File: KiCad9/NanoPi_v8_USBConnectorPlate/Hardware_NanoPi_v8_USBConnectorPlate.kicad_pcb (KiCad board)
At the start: 2 copper layers, 16 x 60 mm, 17 parts, among them J10 Conn_01x04, J11 Conn_01x02, J12 Conn_01x02, J2 USB_Host_Data_02x02, J3 USB_Host_Data_02x02, J4 USB_Power_02x02, J5 Conn_01x03, J6 Conn_01x09, J8 Conn_01x09, U1 USBLC6-2P6, U2 USBLC6-2P6, U3 USBLC6-2P6

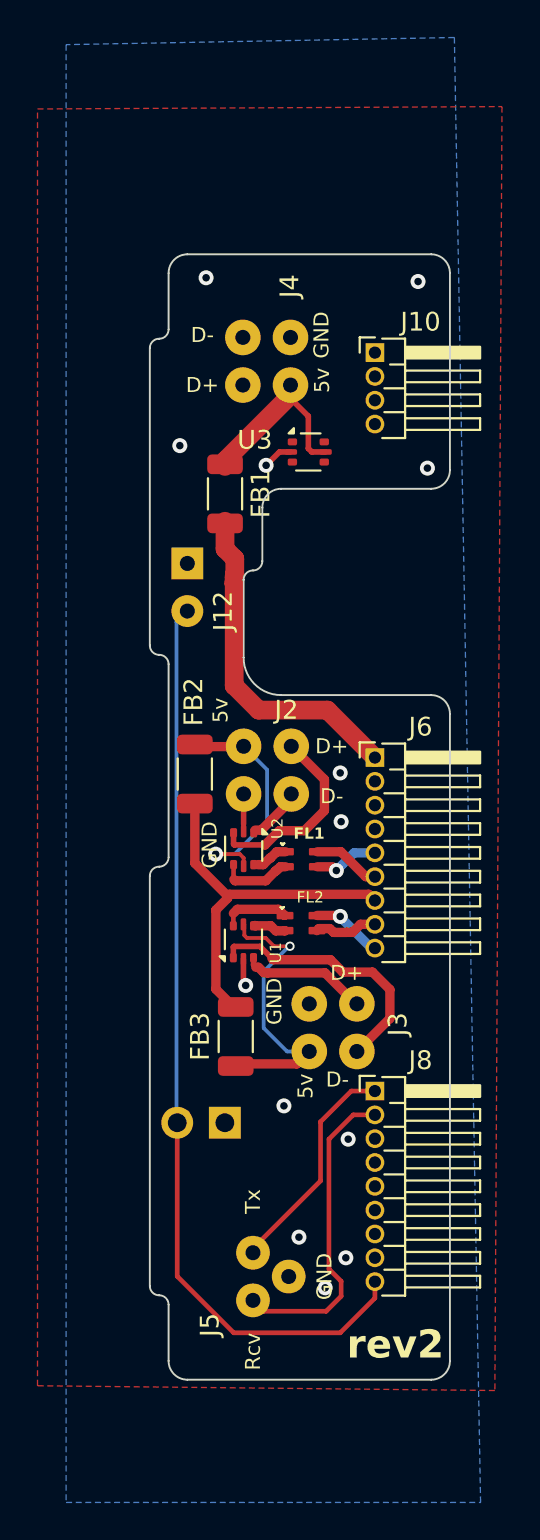
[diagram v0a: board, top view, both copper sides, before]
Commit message: add bom
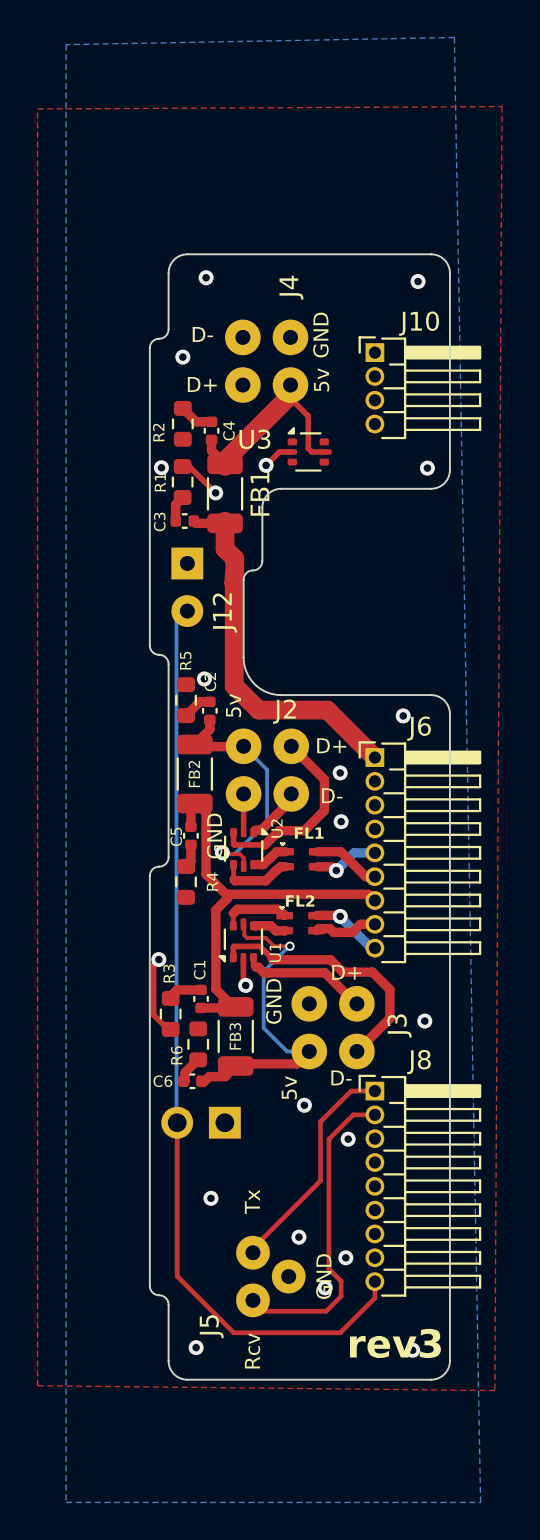
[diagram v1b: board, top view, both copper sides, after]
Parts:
- added C1: 4.7 uF, Capacitor_SMD:C_0402_1005Metric, F.Cu at (104.7, 87.2)
- added C2: 4.7 uF, Capacitor_SMD:C_0402_1005Metric, F.Cu at (105.2, 71.8)
- added C3: 4.7 uF, Capacitor_SMD:C_0402_1005Metric, F.Cu at (103.9, 61.7)
- added C4: 4.7 uF, Capacitor_SMD:C_0402_1005Metric, F.Cu at (105.3, 56.9)
- added C5: 4.7 uF, Capacitor_SMD:C_0402_1005Metric, F.Cu at (104.2, 78.5)
- added C6: 4.7 uF, Capacitor_SMD:C_0402_1005Metric, F.Cu at (104.3, 91.6)
- added R1: 4.7 Ohm, Resistor_SMD:R_0603_1608Metric, F.Cu at (103.8, 59.6)
- added R2: 4.7 Ohm, Resistor_SMD:R_0603_1608Metric, F.Cu at (103.8, 56.5)
- added R3: 4.7 Ohm, Resistor_SMD:R_0603_1608Metric, F.Cu at (103.1, 88.0)
- added R4: 4.7 Ohm, Resistor_SMD:R_0603_1608Metric, F.Cu at (103.9, 81.0)
- added R5: 4.7 Ohm, Resistor_SMD:R_0603_1608Metric, F.Cu at (103.9, 71.3)
- added R6: 4.7 Ohm, Resistor_SMD:R_0603_1608Metric, F.Cu at (104.6, 89.6)
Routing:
- net GND: track 5.07 -> 11.7 mm, vias 13 -> 22
- net VDD_5V: track 20.5 -> 23.7 mm
- net VDD_5V_OUT2: track 15.4 -> 17.6 mm
- net Net-(C1-Pad2): track 0.00 -> 1.91 mm
- net Net-(C4-Pad2): track 0.00 -> 1.83 mm
- net VBUS: track 18.1 -> 19.8 mm
- net VBUS_IN: track 10.6 -> 12.2 mm
- net Net-(C2-Pad2): track 0.00 -> 1.57 mm
- net Net-(C6-Pad2): track 0.00 -> 1.53 mm
- net Net-(C3-Pad1): track 0.00 -> 1.41 mm
- net Net-(C5-Pad2): track 0.00 -> 1.26 mm
- net VDD_5V_OUT1: track 13.7 -> 14.6 mm
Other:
- board text added: "rev3"
- board text removed: "rev2"

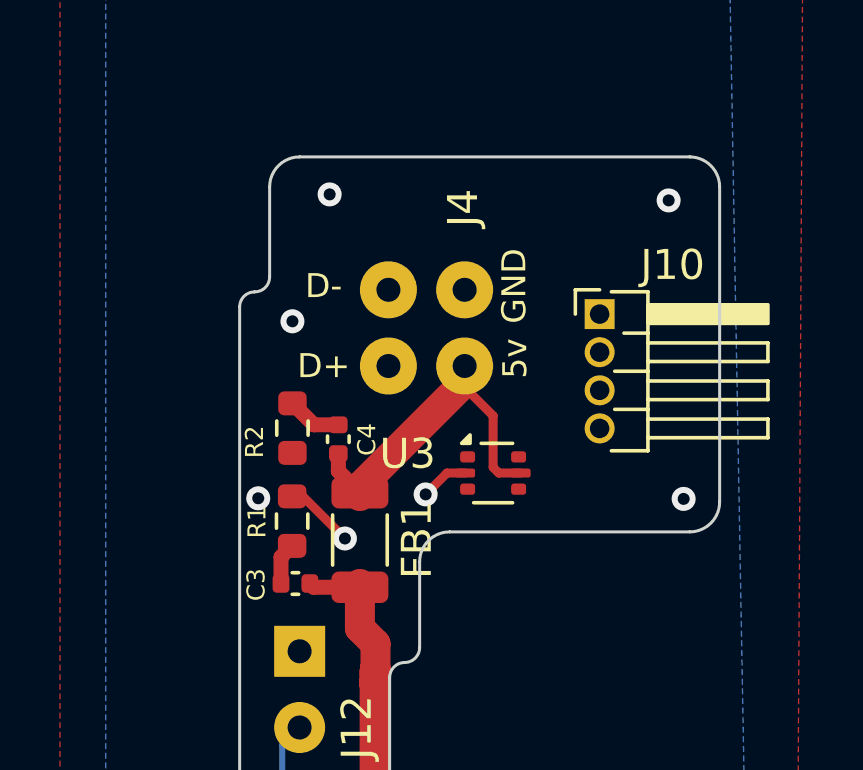
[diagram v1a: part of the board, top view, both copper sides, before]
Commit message: add 3d of wifiboard
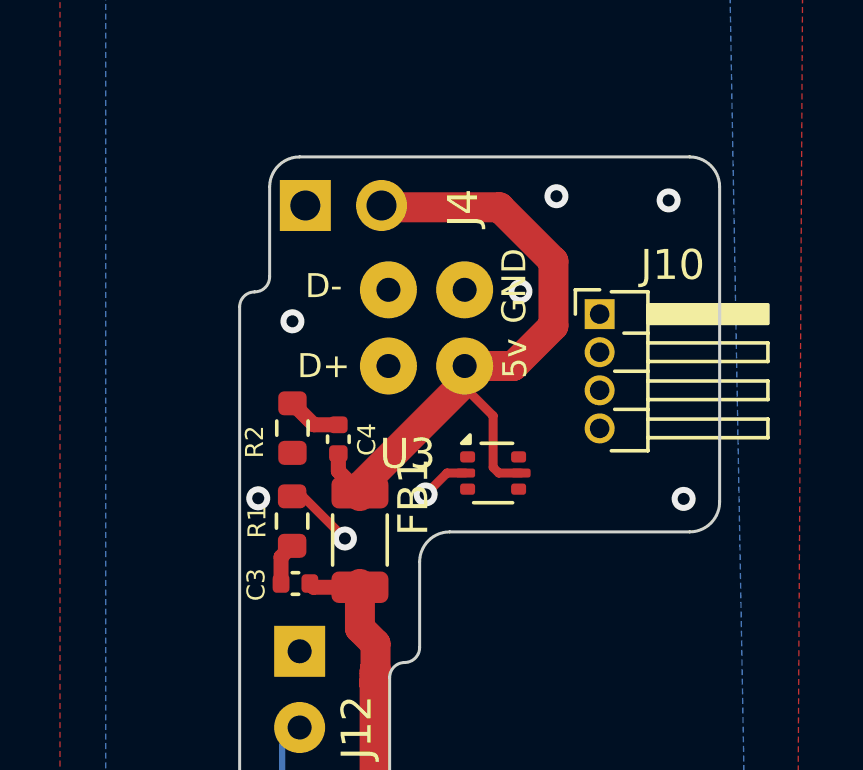
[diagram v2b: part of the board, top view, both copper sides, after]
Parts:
- added J1: Conn_01x02, Connector_PinHeader_2.54mm:PinHeader_1x02_P2.54mm_Horizontal, B.Cu at (104.2, 49.1)
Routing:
- net VBUS_IN: track 12.2 -> 24.5 mm
- net GND: vias 22 -> 23

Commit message: etc
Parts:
- removed FL1, FL2: Choke_CommonMode_FerriteCore_1243, WiRoc:0805_CommonModeChoke
- added FL3: Choke_CommonMode_FerriteCore_1423, WiRoc:0805_CommonModeChoke_1423, F.Cu at (110.0, 79.8)
- added FL4: Choke_CommonMode_FerriteCore_1423, WiRoc:0805_CommonModeChoke_1423, F.Cu at (110.0, 83.0)
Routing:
- net VDD_5V_OUT2: track 17.6 -> 18.9 mm
- net VDD_5V_OUT1: track 14.6 -> 15.5 mm
- net GND: vias 23 -> 24

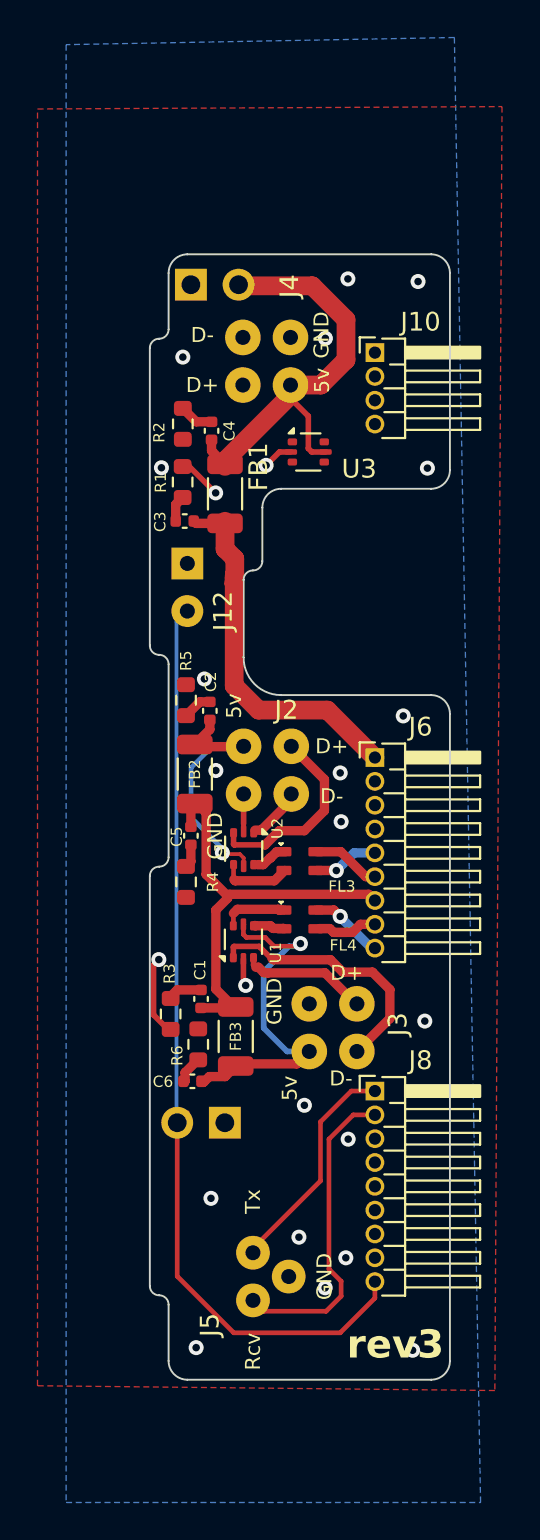
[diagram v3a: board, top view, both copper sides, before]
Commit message: change to use smaller pin holes
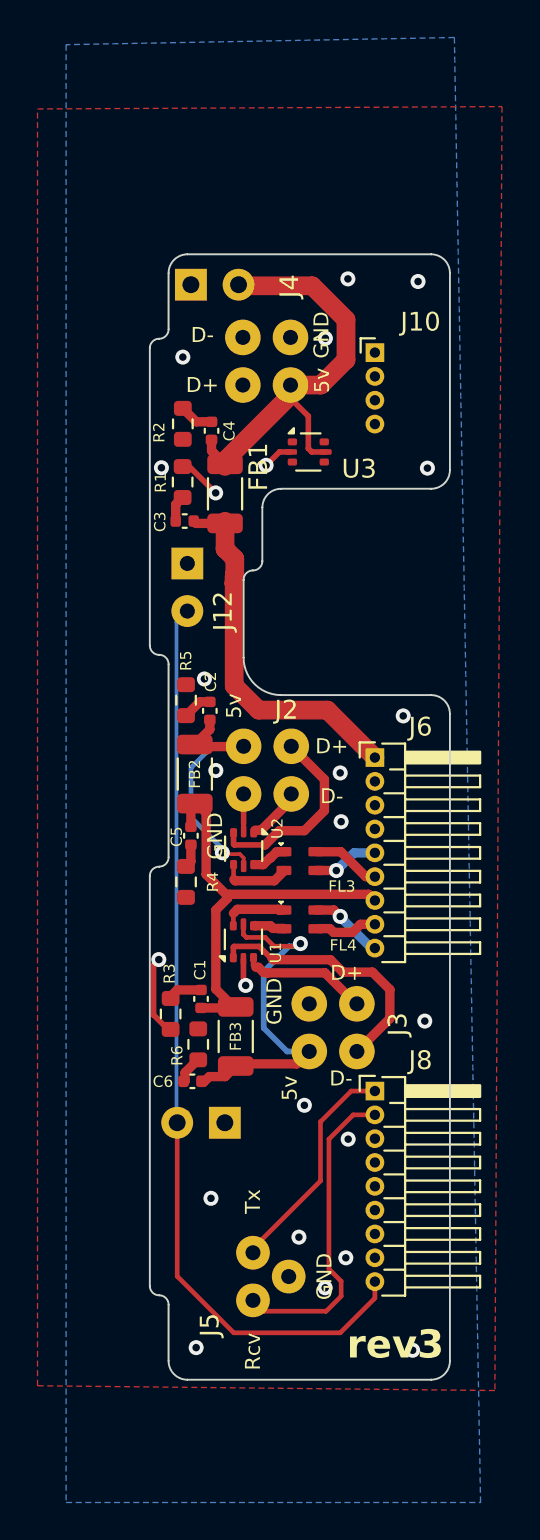
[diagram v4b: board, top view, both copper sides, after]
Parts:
- J1, J11: footprint Connector_PinHeader_2.54mm:PinHeader_1x02_P2.54mm_Horizontal -> WiRoc:PinHeader_1x02_P2.54mm_Horizontal
- J10: footprint Connector_PinHeader_1.27mm:PinHeader_1x04_P1.27mm_Horizontal -> WiRoc:PinHeader_1x04_P1.27mm_Horizontal
- J6, J8: footprint Connector_PinHeader_1.27mm:PinHeader_1x09_P1.27mm_Horizontal -> WiRoc:PinHeader_1x09_P1.27mm_Horizontal

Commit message: add ethernet etc
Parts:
- added C10: 100nF, Capacitor_SMD:C_0402_1005Metric, F.Cu at (104.0, 95.2)
- added C11: 100nF, Capacitor_SMD:C_0402_1005Metric, F.Cu at (104.0, 99.0)
- added C12: 100 nF, Capacitor_SMD:C_0402_1005Metric, B.Cu at (115.8, 102.7)
- added C13: 100 nF, Capacitor_SMD:C_0402_1005Metric, B.Cu at (111.2, 94.3)
- added C14: 1 nF 2kV, Capacitor_SMD:C_1206_3216Metric, B.Cu at (104.3, 105.0)
- added C7: 100nF, Capacitor_SMD:C_0402_1005Metric, F.Cu at (108.3, 93.7)
- added C8: 100nF, Capacitor_SMD:C_0402_1005Metric, F.Cu at (110.7, 93.7)
- added C9: 100nF, Capacitor_SMD:C_0402_1005Metric, F.Cu at (104.0, 97.1)
- added FB4: FerriteBead, Inductor_SMD:L_1206_3216Metric, B.Cu at (103.2, 100.1)
- added FL1: MCZ1210AH900L2TA0G, WiRoc:MCZ1210AH_L2_TDK, B.Cu at (110.2, 105.3)
- added FL2: MCZ1210AH900L2TA0G, WiRoc:MCZ1210AH_L2_TDK, B.Cu at (105.3, 97.7)
- added NT1: NetTie_2, WiRoc:NetTie-2_SMD_Pad0.3mm, B.Cu at (108.4, 103.8)
- added NT2: NetTie_2, WiRoc:NetTie-2_SMD_Pad0.3mm, B.Cu at (107.1, 100.0)
- added R7: 75 Ohm, Resistor_SMD:R_0603_1608Metric, B.Cu at (106.3, 106.0)
- added R8: 75 Ohm, Resistor_SMD:R_0603_1608Metric, B.Cu at (107.8, 106.0)
- added U4: ALT4532M-201-T001, WiRoc:ALT4532M_TDK, B.Cu at (109.2, 96.9)
- added U5: ALT4532M-201-T001, WiRoc:ALT4532M_TDK, B.Cu at (114.3, 105.4)
- added U8: SP3232ECY-L, WiRoc:TSSOP-16_4.4x5mm_P0.65mm_PartOfSilkscreenRemoved, F.Cu at (108.8, 96.9)
- J1, J11: footprint WiRoc:PinHeader_1x02_P2.54mm_Horizontal -> Connector_PinHeader_2.54mm:PinHeader_1x02_P2.54mm_Horizontal
- J10: footprint WiRoc:PinHeader_1x04_P1.27mm_Horizontal -> Connector_PinHeader_1.27mm:PinHeader_1x04_P1.27mm_Horizontal
- J5: value Conn_01x03 -> Conn_01x05; footprint WiRoc:SerialConnPads3Pin -> WiRoc:SerialAndEthConnPads4Pin
- J6, J8: footprint WiRoc:PinHeader_1x09_P1.27mm_Horizontal -> Connector_PinHeader_1.27mm:PinHeader_1x09_P1.27mm_Horizontal
- moved J11 0.80 mm to (106.0, 93.0)
- moved J5 0.72 mm to (108.1, 101.6)
- moved C1 0.30 mm to (104.8, 86.9)
- moved C6 0.30 mm to (104.3, 91.3)
- moved FB3 0.30 mm to (106.6, 88.9)
- moved R3 0.30 mm to (103.1, 87.7)
- moved R6 0.30 mm to (104.6, 89.3)
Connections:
- J5 pad 1: R2IN -> UART2_RX
- J5 pad 2: T2OUT -> UART2_TX
- J8 pad 4: unconnected-(J8-Pin_4-Pad4) -> EPHY-RXP
- J8 pad 5: unconnected-(J8-Pin_5-Pad5) -> EPHY-RXN
- J8 pad 6: unconnected-(J8-Pin_6-Pad6) -> EPHY-TXP
- J8 pad 7: unconnected-(J8-Pin_7-Pad7) -> EPHY-TXN
- J8 pad 8: GND -> SYS_3.3V
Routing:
- net Net-(R7-Pad1): track 0.00 -> 11.5 mm
- net EPHY-TXP: track 0.00 -> 11.5 mm
- net EPHY-TXN: track 0.00 -> 11.4 mm
- net SYS_3.3V: track 0.00 -> 9.41 mm, vias 0 -> 1
- net R2IN: track 16.9 -> 10.3 mm
- net CABLE-RXP: track 0.00 -> 5.99 mm
- net Net-(C14-Pad1): track 0.00 -> 5.83 mm
- net Net-(R8-Pad1): track 0.00 -> 5.32 mm
- net UART2_RX: track 0.00 -> 4.59 mm
- net GND: track 11.7 -> 16.3 mm, vias 24 -> 44
- net Net-(U8-C1-): track 0.00 -> 4.11 mm
- net CABLE-RXN: track 0.00 -> 4.10 mm
- net EPHY-RXP: track 0.00 -> 3.65 mm
- net EPHY-RXN: track 0.00 -> 3.62 mm
- net UART2_TX: track 0.00 -> 3.51 mm
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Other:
- board text added: "rev4"
- board text removed: "rev3"
